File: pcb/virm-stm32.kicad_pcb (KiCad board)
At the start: 2 copper layers, 89 parts, among them J1 Conn_02x10, J2 Conn_01x04, J3 TYPE-C-31-M-12, SW1 SW_SPDT, SW2 SW_Push, SW3 SW_Push, SW4 SW_Push, U1 STM32F070CBTx, U2 XC6206P332MR, Y1 16MHz

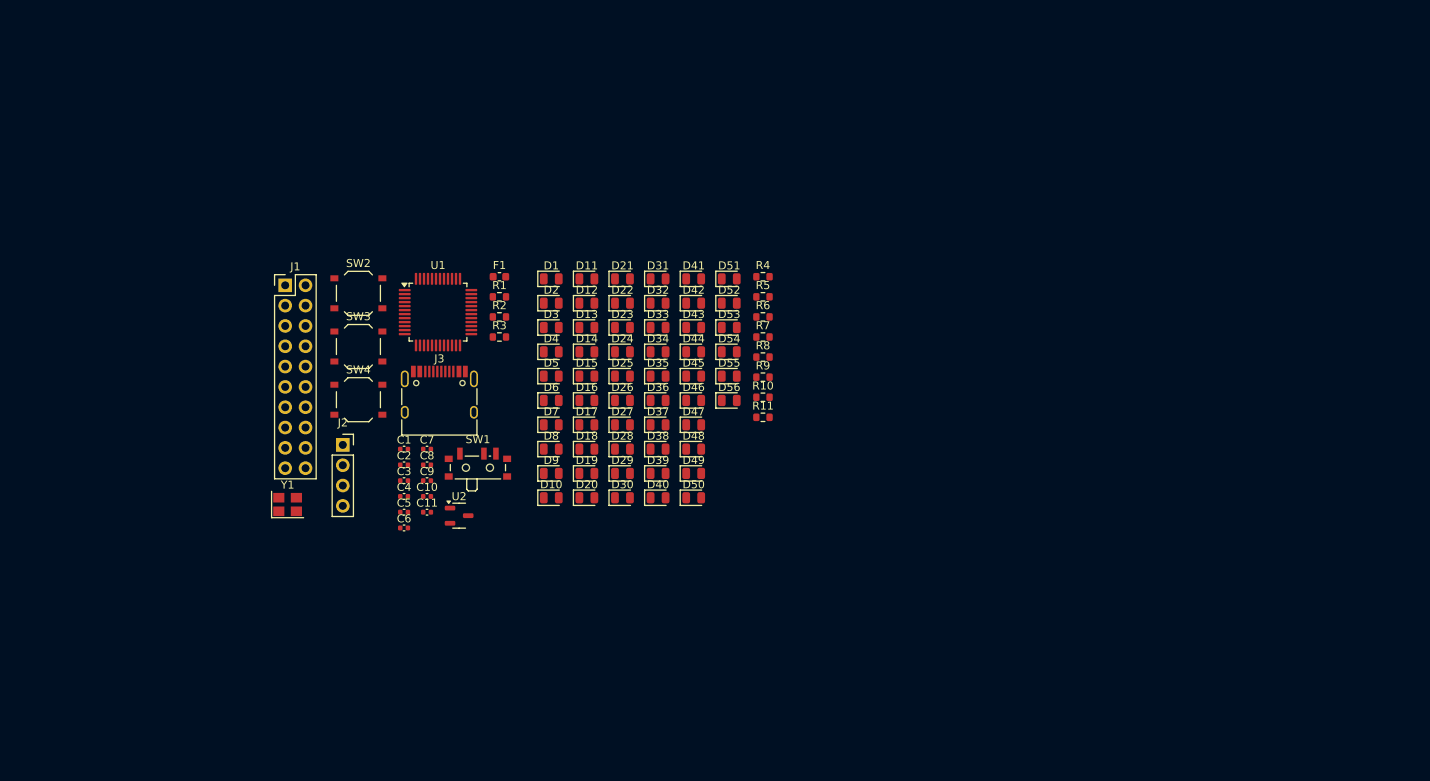
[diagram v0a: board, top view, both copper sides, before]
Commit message: Started working on PCB layout
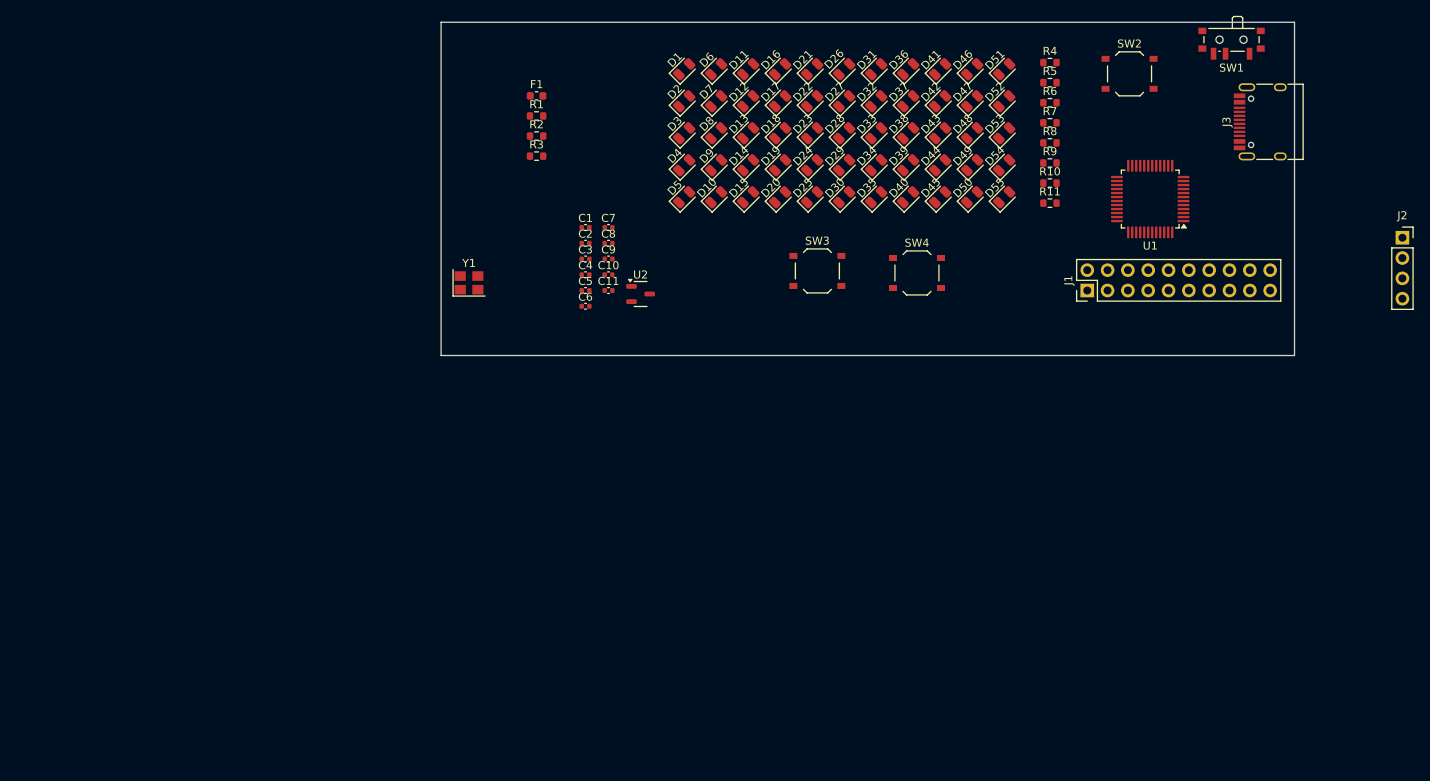
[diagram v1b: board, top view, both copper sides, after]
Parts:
- removed D56: LED_Small, LED_SMD:LED_0805_2012Metric
- moved J2 135.0 mm to (219.7, 58.9)
- moved J3 109.9 mm to (203.4, 44.5), turned to 90 degrees
- moved SW1 108.0 mm to (198.4, 34.5), turned to 180 degrees
- moved J1 100.3 mm to (180.3, 65.5), turned to 90 degrees
- moved SW2 100.2 mm to (185.6, 38.5)
- moved U1 90.1 mm to (188.2, 54.1), turned to 180 degrees
- moved SW4 71.6 mm to (159.1, 63.3)
- moved SW3 58.1 mm to (146.6, 63.1)
- moved D46 54.1 mm to (166.0, 37.9), turned to 45 degrees
- moved D47 53.4 mm to (166.0, 41.9), turned to 45 degrees
- moved D48 52.6 mm to (166.0, 45.9), turned to 45 degrees
- moved D49 51.9 mm to (166.0, 49.9), turned to 45 degrees
- moved D36 51.9 mm to (158.0, 37.9), turned to 45 degrees
- moved D50 51.2 mm to (166.0, 53.9), turned to 45 degrees
- moved D37 51.1 mm to (158.0, 41.9), turned to 45 degrees
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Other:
- board outline added: 106.7 x 41.7 mm
- rule pad_to_mask_clearance: 0 -> 0.038

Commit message: started routing, with additional leds
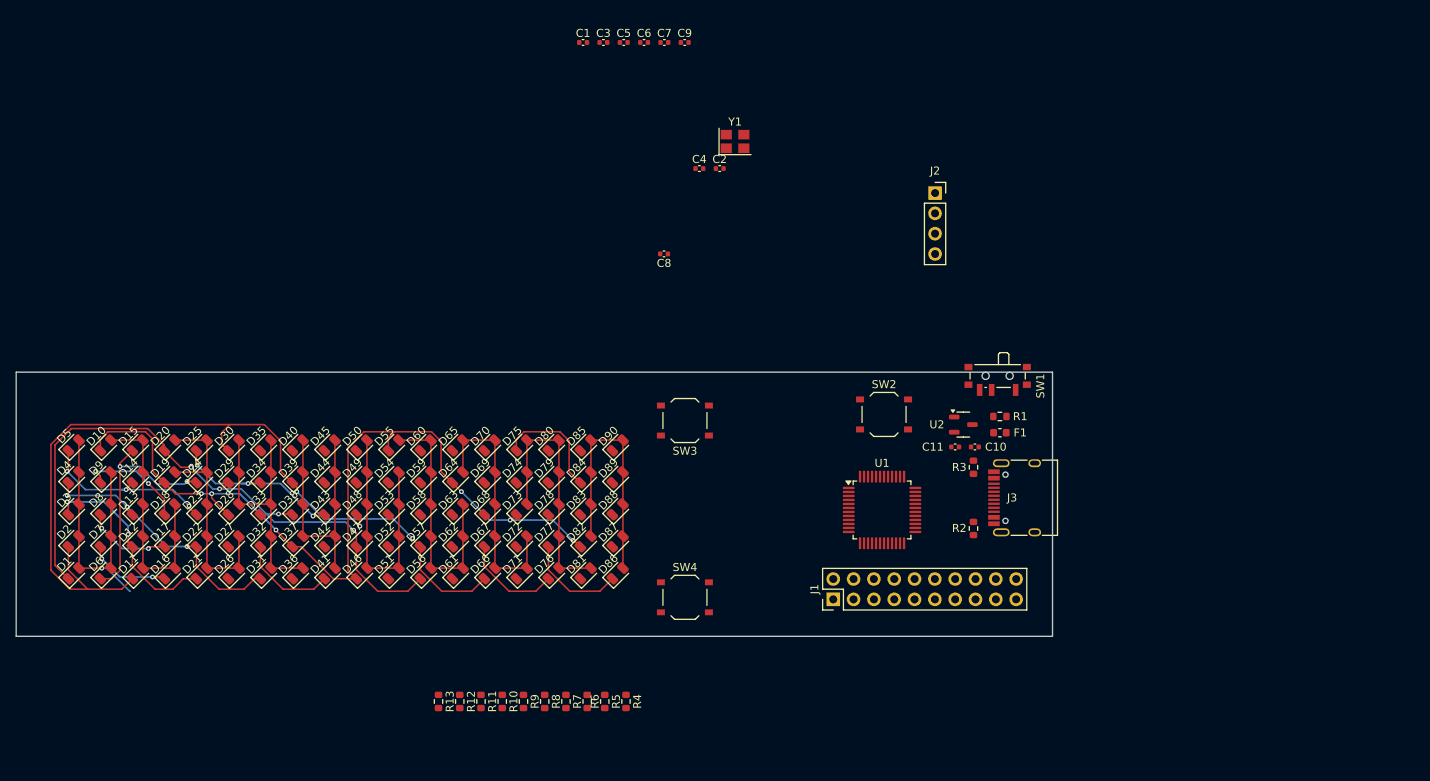
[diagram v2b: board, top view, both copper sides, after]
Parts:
- added D56: LED_Small, LED_SMD:LED_0805_2012Metric, F.Cu at (97.6, 100.9)
- added D57: LED_Small, LED_SMD:LED_0805_2012Metric, F.Cu at (97.6, 96.9)
- added D58: LED_Small, LED_SMD:LED_0805_2012Metric, F.Cu at (97.6, 92.9)
- added D59: LED_Small, LED_SMD:LED_0805_2012Metric, F.Cu at (97.6, 88.9)
- added D60: LED_Small, LED_SMD:LED_0805_2012Metric, F.Cu at (97.6, 84.9)
- added D61: LED_Small, LED_SMD:LED_0805_2012Metric, F.Cu at (101.6, 100.9)
- added D62: LED_Small, LED_SMD:LED_0805_2012Metric, F.Cu at (101.6, 96.9)
- added D63: LED_Small, LED_SMD:LED_0805_2012Metric, F.Cu at (101.6, 92.9)
- added D64: LED_Small, LED_SMD:LED_0805_2012Metric, F.Cu at (101.6, 88.9)
- added D65: LED_Small, LED_SMD:LED_0805_2012Metric, F.Cu at (101.6, 84.9)
- added D66: LED_Small, LED_SMD:LED_0805_2012Metric, F.Cu at (105.6, 100.9)
- added D67: LED_Small, LED_SMD:LED_0805_2012Metric, F.Cu at (105.6, 96.9)
- added D68: LED_Small, LED_SMD:LED_0805_2012Metric, F.Cu at (105.6, 92.9)
- added D69: LED_Small, LED_SMD:LED_0805_2012Metric, F.Cu at (105.6, 88.9)
- added D70: LED_Small, LED_SMD:LED_0805_2012Metric, F.Cu at (105.6, 84.9)
- added D71: LED_Small, LED_SMD:LED_0805_2012Metric, F.Cu at (109.6, 100.9)
- added D72: LED_Small, LED_SMD:LED_0805_2012Metric, F.Cu at (109.6, 96.9)
- added D73: LED_Small, LED_SMD:LED_0805_2012Metric, F.Cu at (109.6, 92.9)
- added D74: LED_Small, LED_SMD:LED_0805_2012Metric, F.Cu at (109.6, 88.9)
- added D75: LED_Small, LED_SMD:LED_0805_2012Metric, F.Cu at (109.6, 84.9)
- added D76: LED_Small, LED_SMD:LED_0805_2012Metric, F.Cu at (113.6, 100.9)
- added D77: LED_Small, LED_SMD:LED_0805_2012Metric, F.Cu at (113.6, 96.9)
- added D78: LED_Small, LED_SMD:LED_0805_2012Metric, F.Cu at (113.6, 92.9)
- added D79: LED_Small, LED_SMD:LED_0805_2012Metric, F.Cu at (113.6, 88.9)
- added D80: LED_Small, LED_SMD:LED_0805_2012Metric, F.Cu at (113.6, 84.9)
- added D81: LED_Small, LED_SMD:LED_0805_2012Metric, F.Cu at (117.6, 100.9)
- added D82: LED_Small, LED_SMD:LED_0805_2012Metric, F.Cu at (117.6, 96.9)
- added D83: LED_Small, LED_SMD:LED_0805_2012Metric, F.Cu at (117.6, 92.9)
- added D84: LED_Small, LED_SMD:LED_0805_2012Metric, F.Cu at (117.6, 88.9)
- added D85: LED_Small, LED_SMD:LED_0805_2012Metric, F.Cu at (117.6, 84.9)
- added D86: LED_Small, LED_SMD:LED_0805_2012Metric, F.Cu at (121.6, 100.9)
- added D87: LED_Small, LED_SMD:LED_0805_2012Metric, F.Cu at (121.6, 96.9)
- added D88: LED_Small, LED_SMD:LED_0805_2012Metric, F.Cu at (121.6, 92.9)
- added D89: LED_Small, LED_SMD:LED_0805_2012Metric, F.Cu at (121.6, 88.9)
- added D90: LED_Small, LED_SMD:LED_0805_2012Metric, F.Cu at (121.6, 84.9)
- added R12: 51Ω, Resistor_SMD:R_0603_1608Metric, F.Cu at (101.9, 116.9)
- added R13: 51Ω, Resistor_SMD:R_0603_1608Metric, F.Cu at (99.2, 116.9)
- moved D16 99.0 mm to (65.6, 100.9)
- moved D21 99.0 mm to (69.6, 100.9)
- moved D26 99.0 mm to (73.6, 100.9)
- moved D31 99.0 mm to (77.6, 100.9)
- moved D36 99.0 mm to (81.6, 100.9)
- moved D41 99.0 mm to (85.6, 100.9)
- moved D46 99.0 mm to (89.6, 100.9)
- moved D51 99.0 mm to (93.6, 100.9)
- moved D1 99.0 mm to (53.6, 100.9)
- moved D11 99.0 mm to (61.6, 100.9)
- moved D6 99.0 mm to (57.6, 100.9)
- moved R4 95.8 mm to (122.7, 116.9), turned to -90 degrees
- moved R5 95.3 mm to (120.0, 116.9), turned to -90 degrees
- moved R6 94.6 mm to (117.8, 116.9), turned to -90 degrees
- moved R11 94.5 mm to (104.6, 116.9), turned to -90 degrees
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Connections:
- D10 pad 1: LED3 -> LED0
- D11 pad 1: LED4 -> LED2
- D12 pad 1: LED5 -> LED3
- D13 pad 1: LED6 -> LED4
- D14 pad 1: LED7 -> LED5
- D15 pad 1: LED0 -> LED6
- D15 pad 2: Net-(D15-A) -> Net-(D10-A)
- D16 pad 1: LED1 -> LED7
- D16 pad 2: Net-(D15-A) -> Net-(D10-A)
- D17 pad 1: LED3 -> LED8
- D17 pad 2: Net-(D15-A) -> Net-(D10-A)
- D18 pad 1: LED4 -> LED9
- D18 pad 2: Net-(D15-A) -> Net-(D10-A)
- D19 pad 1: LED5 -> LED0
- D19 pad 2: Net-(D15-A) -> Net-(D19-A)
- D20 pad 1: LED6 -> LED1
- D20 pad 2: Net-(D15-A) -> Net-(D19-A)
- D21 pad 1: LED7 -> LED3
- D21 pad 2: Net-(D15-A) -> Net-(D19-A)
- D22 pad 1: LED0 -> LED4
- D22 pad 2: Net-(D22-A) -> Net-(D19-A)
- D23 pad 1: LED1 -> LED5
- D23 pad 2: Net-(D22-A) -> Net-(D19-A)
- D24 pad 1: LED2 -> LED6
- D24 pad 2: Net-(D22-A) -> Net-(D19-A)
- D25 pad 1: LED4 -> LED7
- D25 pad 2: Net-(D22-A) -> Net-(D19-A)
- D26 pad 1: LED5 -> LED8
- D26 pad 2: Net-(D22-A) -> Net-(D19-A)
- D27 pad 1: LED6 -> LED9
- D27 pad 2: Net-(D22-A) -> Net-(D19-A)
- D28 pad 1: LED7 -> LED0
- D28 pad 2: Net-(D22-A) -> Net-(D28-A)
- D29 pad 1: LED0 -> LED1
- D29 pad 2: Net-(D29-A) -> Net-(D28-A)
- D30 pad 1: LED1 -> LED2
- D30 pad 2: Net-(D29-A) -> Net-(D28-A)
- D31 pad 1: LED2 -> LED4
- D31 pad 2: Net-(D29-A) -> Net-(D28-A)
- D32 pad 1: LED3 -> LED5
- D32 pad 2: Net-(D29-A) -> Net-(D28-A)
- D33 pad 1: LED5 -> LED6
- D33 pad 2: Net-(D29-A) -> Net-(D28-A)
- D34 pad 1: LED6 -> LED7
- D34 pad 2: Net-(D29-A) -> Net-(D28-A)
- D35 pad 1: LED7 -> LED8
- D35 pad 2: Net-(D29-A) -> Net-(D28-A)
- D36 pad 1: LED0 -> LED9
- D36 pad 2: Net-(D36-A) -> Net-(D28-A)
- D37 pad 1: LED1 -> LED0
- D37 pad 2: Net-(D36-A) -> Net-(D37-A)
- D38 pad 1: LED2 -> LED1
- D38 pad 2: Net-(D36-A) -> Net-(D37-A)
- D39 pad 1: LED3 -> LED2
- D39 pad 2: Net-(D36-A) -> Net-(D37-A)
- D40 pad 1: LED4 -> LED3
- D40 pad 2: Net-(D36-A) -> Net-(D37-A)
- D41 pad 1: LED6 -> LED5
- D41 pad 2: Net-(D36-A) -> Net-(D37-A)
- D42 pad 1: LED7 -> LED6
- D42 pad 2: Net-(D36-A) -> Net-(D37-A)
- D43 pad 1: LED0 -> LED7
- D43 pad 2: Net-(D43-A) -> Net-(D37-A)
- D44 pad 1: LED1 -> LED8
- D44 pad 2: Net-(D43-A) -> Net-(D37-A)
- D45 pad 1: LED2 -> LED9
- D45 pad 2: Net-(D43-A) -> Net-(D37-A)
- D46 pad 1: LED3 -> LED0
- D46 pad 2: Net-(D43-A) -> Net-(D46-A)
- D47 pad 1: LED4 -> LED1
- D47 pad 2: Net-(D43-A) -> Net-(D46-A)
- D48 pad 1: LED5 -> LED2
- D48 pad 2: Net-(D43-A) -> Net-(D46-A)
- D49 pad 1: LED7 -> LED3
- D49 pad 2: Net-(D43-A) -> Net-(D46-A)
- D50 pad 1: LED0 -> LED4
- D50 pad 2: Net-(D50-A) -> Net-(D46-A)
- D51 pad 1: LED1 -> LED6
- D51 pad 2: Net-(D50-A) -> Net-(D46-A)
- D52 pad 1: LED2 -> LED7
- D52 pad 2: Net-(D50-A) -> Net-(D46-A)
- D53 pad 1: LED3 -> LED8
- D53 pad 2: Net-(D50-A) -> Net-(D46-A)
- D54 pad 1: LED4 -> LED9
- D54 pad 2: Net-(D50-A) -> Net-(D46-A)
- D55 pad 1: LED5 -> LED0
- D55 pad 2: Net-(D50-A) -> Net-(D55-A)
- D8 pad 1: LED0 -> LED8
- D8 pad 2: Net-(D10-A) -> Net-(D1-A)
- D9 pad 1: LED2 -> LED9
- D9 pad 2: Net-(D10-A) -> Net-(D1-A)
- R10 pad 2: Net-(D43-A) -> Net-(D55-A)
- R11 pad 2: Net-(D50-A) -> Net-(D64-A)
- R6 pad 2: Net-(D15-A) -> Net-(D19-A)
- R7 pad 2: Net-(D22-A) -> Net-(D28-A)
- R8 pad 2: Net-(D29-A) -> Net-(D37-A)
- R9 pad 2: Net-(D36-A) -> Net-(D46-A)
- U1 pad 29: unconnected-(U1-PA8-Pad29) -> LED8
- U1 pad 30: unconnected-(U1-PA9-Pad30) -> LED9
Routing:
- net LED2: track 0.00 -> 125.0 mm, vias 0 -> 3
- net LED0: track 0.00 -> 105.8 mm, vias 0 -> 6
- net LED1: track 0.00 -> 81.0 mm, vias 0 -> 4
- net LED4: track 0.00 -> 46.5 mm, vias 0 -> 3
- net LED3: track 0.00 -> 37.9 mm, vias 0 -> 2
- net Net-(D1-A): track 0.00 -> 36.8 mm, vias 0 -> 1
- net LED5: track 0.00 -> 35.0 mm, vias 0 -> 3
- net LED7: track 0.00 -> 33.2 mm, vias 0 -> 5
- net Net-(D28-A): track 0.00 -> 32.0 mm
- net Net-(D64-A): track 0.00 -> 32.0 mm
- net Net-(D73-A): track 0.00 -> 32.0 mm
- net Net-(D55-A): track 0.00 -> 32.0 mm
- net Net-(D82-A): track 0.00 -> 32.0 mm
- net Net-(D46-A): track 0.00 -> 32.0 mm
- net Net-(D37-A): track 0.00 -> 32.0 mm
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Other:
- board size 106.7 x 41.7 mm -> 129.5 x 33 mm

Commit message: First attempt at routing, also move the serial wire debug to the same header as the other IO's
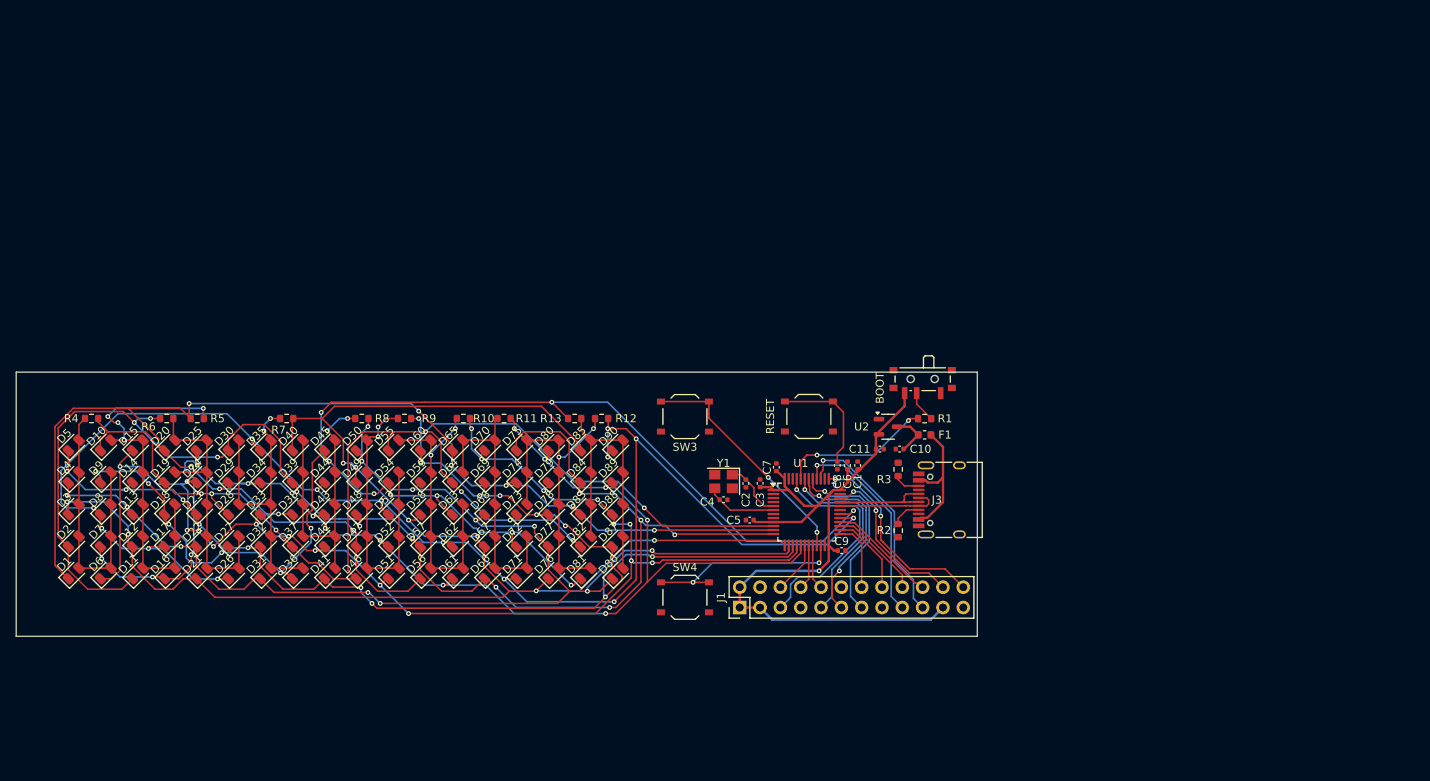
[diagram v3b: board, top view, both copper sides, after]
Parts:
- removed J2: Conn_01x04, Connector_PinSocket_2.54mm:PinSocket_1x04_P2.54mm_Vertical
- removed SW1: SW_SPDT, Button_Switch_SMD:SW_SPDT_PCM12
- removed SW2: SW_Push, Button_Switch_SMD:SW_Push_1P1T_XKB_TS-1187A
- added BOOT: SW_SPDT, Button_Switch_SMD:SW_SPDT_PCM12, F.Cu at (159.8, 76.9)
- added RESET: SW_Push, Button_Switch_SMD:SW_Push_1P1T_XKB_TS-1187A, F.Cu at (145.5, 81.3)
- J1: value Conn_02x10 -> Conn_02x12_Odd_Even; footprint Connector_PinHeader_2.54mm:PinHeader_2x10_P2.54mm_Vertical -> Connector_PinHeader_2.54mm:PinHeader_2x12_P2.54mm_Vertical
- moved R4 75.6 mm to (55.9, 81.5), turned to 180 degrees
- moved C9 66.5 mm to (149.6, 98.0)
- moved R6 63.3 mm to (65.3, 81.5), turned to 0 degrees
- moved C1 63.0 mm to (151.6, 87.4), turned to 90 degrees
- moved R5 62.0 mm to (69.1, 81.5), turned to 0 degrees
- moved C5 61.7 mm to (138.1, 94.2), turned to 180 degrees
- moved C6 58.7 mm to (150.4, 87.4), turned to 90 degrees
- moved C3 58.5 mm to (139.4, 89.6), turned to 90 degrees
- moved C7 54.9 mm to (141.5, 87.6), turned to 90 degrees
- moved R7 49.7 mm to (80.3, 81.5), turned to 180 degrees
- moved Y1 42.5 mm to (134.9, 89.4), turned to 180 degrees
- moved R8 42.1 mm to (89.7, 81.5), turned to 180 degrees
- moved C4 41.5 mm to (134.9, 91.7)
- moved R12 39.6 mm to (119.6, 81.5), turned to 180 degrees
- moved C2 39.5 mm to (137.7, 89.7), turned to -90 degrees
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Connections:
- J3 pad A1: (no net) -> GND
- J3 pad A12: (no net) -> GND
- J3 pad A4: (no net) -> +5V
- J3 pad A9: (no net) -> +5V
- J3 pad B1: (no net) -> GND
- J3 pad B12: (no net) -> GND
- J3 pad B4: (no net) -> +5V
- J3 pad B9: (no net) -> +5V
- U1 pad 34: /SWDIO -> SWDIO
- U1 pad 37: /SWCLK -> SWCLK
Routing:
- net LED8: track 10.7 -> 189.0 mm, vias 2 -> 14
- net LED9: track 13.6 -> 188.5 mm, vias 2 -> 15
- net LED3: track 37.9 -> 188.3 mm, vias 2 -> 8
- net LED6: track 29.2 -> 163.2 mm, vias 2 -> 18
- net LED7: track 33.2 -> 158.0 mm, vias 5 -> 14
- net LED5: track 35.0 -> 158.9 mm, vias 3 -> 15
- net LED4: track 46.5 -> 153.9 mm, vias 3 -> 12
- net LED1: track 81.0 -> 179.2 mm, vias 4 -> 10
- net +3.3V: track 0.00 -> 94.1 mm, vias 0 -> 1
- net LED2: track 125.0 -> 180.3 mm, vias 3 -> 11
- net LED0: track 105.8 -> 157.3 mm, vias 6 -> 8
- net BTN0: track 0.00 -> 29.6 mm, vias 0 -> 2
- net PB8: track 0.00 -> 28.2 mm, vias 0 -> 1
- net PB3: track 0.00 -> 27.4 mm, vias 0 -> 1
- net PB4: track 0.00 -> 25.8 mm, vias 0 -> 1
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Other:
- board size 129.5 x 33 mm -> 120.1 x 33 mm

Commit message: Added new board outline
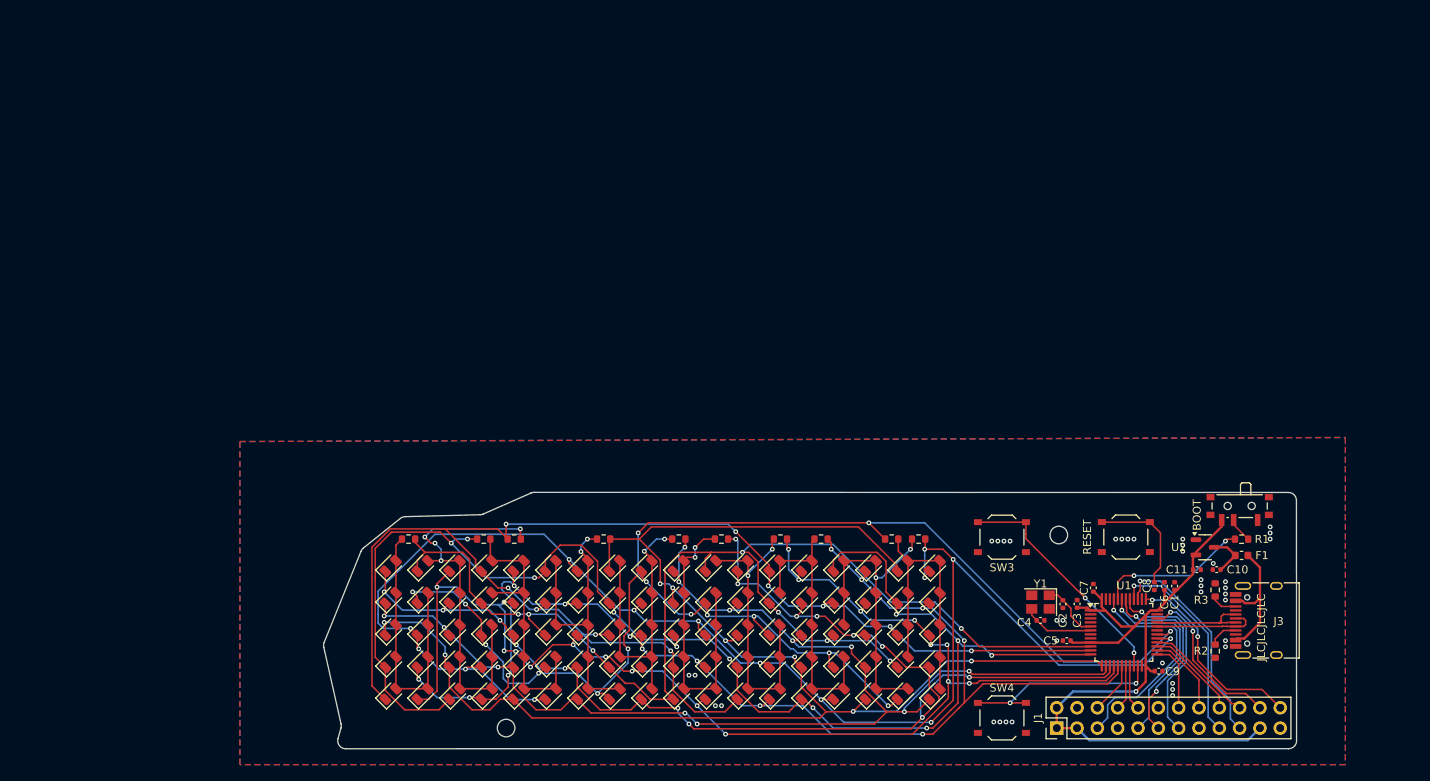
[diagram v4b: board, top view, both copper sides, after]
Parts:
- added REF**: MountingHole_2.2mm_M2, MountingHole:MountingHole_2.2mm_M2, F.Cu at (107.7, 120.2)
- added REF**: MountingHole_2.2mm_M2, MountingHole:MountingHole_2.2mm_M2, F.Cu at (176.8, 96.1)
- moved BOOT 42.7 mm to (199.4, 92.8)
- moved U1 42.4 mm to (184.9, 108.3)
- moved C11 42.4 mm to (194.0, 100.4)
- moved C9 42.4 mm to (189.3, 113.1)
- moved R3 42.4 mm to (196.3, 103.0)
- moved R2 42.4 mm to (196.3, 110.6)
- moved D16 42.4 mm to (105.3, 116.0)
- moved D17 42.4 mm to (105.3, 112.0)
- moved D18 42.4 mm to (105.3, 108.0)
- moved D19 42.4 mm to (105.3, 104.0)
- moved D20 42.4 mm to (105.3, 100.0)
- moved D21 42.4 mm to (109.3, 116.0)
- moved D22 42.4 mm to (109.3, 112.0)
- moved D23 42.4 mm to (109.3, 108.0)
- moved D24 42.4 mm to (109.3, 104.0)
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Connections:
- J3 pad A1: GND -> (no net)
- J3 pad A12: GND -> (no net)
- J3 pad A4: +5V -> (no net)
- J3 pad A9: +5V -> (no net)
- J3 pad B1: GND -> (no net)
- J3 pad B12: GND -> (no net)
- J3 pad B4: +5V -> (no net)
- J3 pad B9: +5V -> (no net)
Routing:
- net +3.3V: track 94.1 -> 93.3 mm
- net Net-(SW1-B): track 3.94 -> 3.14 mm
- net GND: vias 0 -> 39
- added copper zone on B.Cu, net GND
- added copper zone on F.Cu, net GND
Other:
- board size 120.1 x 33 mm -> 121.6 x 32.1 mm
- board text added: "Casteel"
- board text added: "JLCJLCJLCJLC"
- board text added: "Martijn"
